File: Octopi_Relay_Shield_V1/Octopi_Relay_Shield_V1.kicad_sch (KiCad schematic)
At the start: 12 parts, among them J1 Raspberry_Pi_2_3, J2 Screw_Terminal_01x03, K1 JQC-3FF-005-1Z, Q1 PNP, U1 LTV-817S

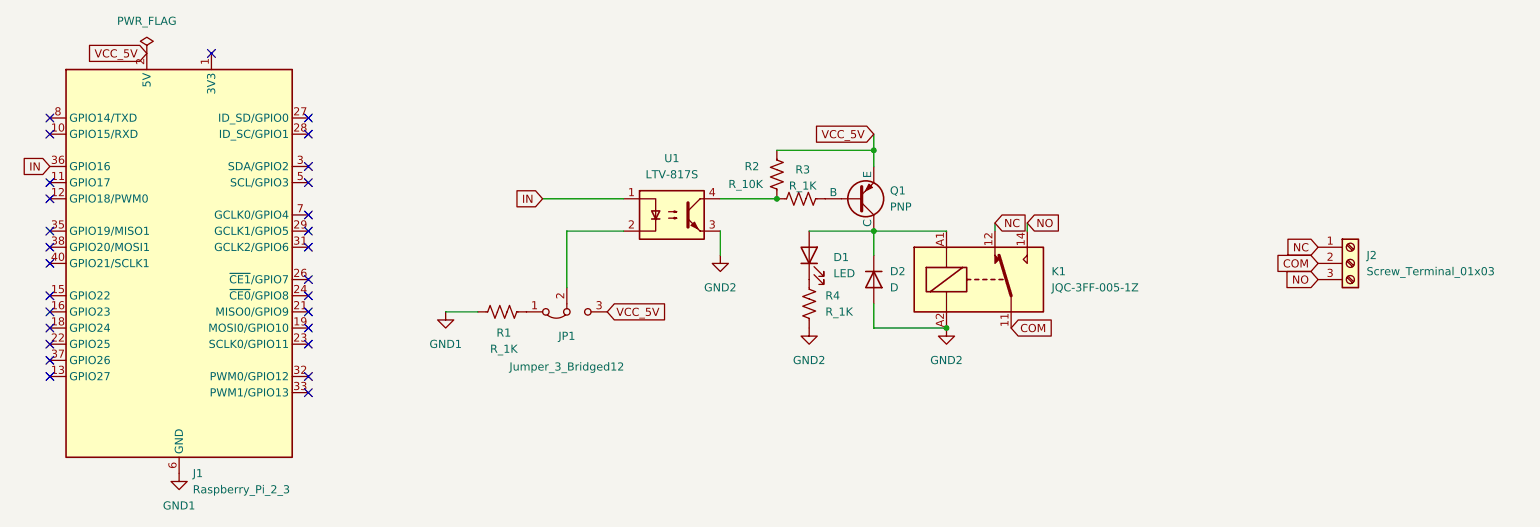
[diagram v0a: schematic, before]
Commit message: Completed Layout for first two designs, generated the fab files
updated the nets, GND1 and GND2 have been joined into just GND1. separated GNDs would only be possible if there was a separate non-pi voltage source for the 5V on the other side of the octocoupler
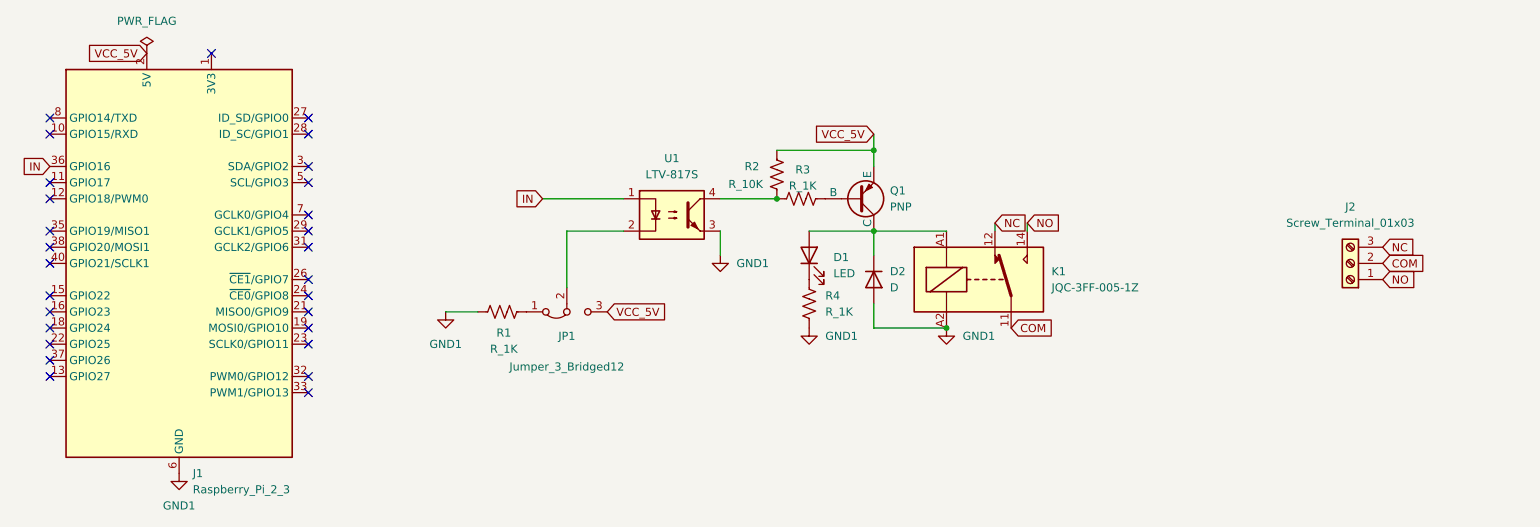
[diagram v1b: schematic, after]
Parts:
- D1: footprint (none) -> LED_SMD:LED_0603_1608Metric_Pad1.05x0.95mm_HandSolder
- D2: footprint (none) -> Diode_THT:D_5W_P12.70mm_Horizontal
- J1: footprint (none) -> Connector_PinSocket_2.54mm:PinSocket_2x20_P2.54mm_Vertical
- J2: footprint (none) -> TerminalBlock_Phoenix:TerminalBlock_Phoenix_PT-1,5-3-5.0-H_1x03_P5.00mm_Horizontal
- JP1: footprint (none) -> Connector_PinHeader_2.54mm:PinHeader_1x03_P2.54mm_Vertical
- Q1: footprint (none) -> Package_TO_SOT_SMD:SOT-23_Handsoldering
- R1, R2, R3, R4: footprint (none) -> Resistor_SMD:R_0805_2012Metric_Pad1.20x1.40mm_HandSolder
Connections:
- net GND2 is gone; now on net GND1: D2.2 (A), K1.A2, R4.2, U1.3
- net NC: now also J2.3 (Pin_3); no longer J2.1 (Pin_1)
- net NO: now also J2.1 (Pin_1); no longer J2.3 (Pin_3)
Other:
- moved on the sheet: J2
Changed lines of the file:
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@@
 	(global_label "COM"
 		(shape input)
-		(at 229.87 74.93 180)
+		(at 240.03 74.93 0)
 		(fields_autoplaced yes)
 		(effects
@@
 				(size 1.27 1.27)
 			)
-			(justify right)
+			(justify left)
 		)
 		(property "Intersheetrefs" "${INTERSHEET_REFS}"
-			(at 222.8329 74.93 0)
-			(effects
-				(font
-					(size 1.27 1.27)
-				)
-				(justify right)
+			(at 247.0671 74.93 0)
+			(effects
+				(font
+					(size 1.27 1.27)
+				)
+				(justify left)
 				(hide yes)
 			)
@@
 	(global_label "NC"
 		(shape input)
-		(at 229.87 72.39 180)
+		(at 240.03 72.39 0)
 		(fields_autoplaced yes)
 		(effects
@@
 				(size 1.27 1.27)
 			)
-			(justify right)
+			(justify left)
 		)
 		(property "Intersheetrefs" "${INTERSHEET_REFS}"
-			(at 224.2843 72.39 0)
-			(effects
-				(font
-					(size 1.27 1.27)
-				)
-				(justify right)
+			(at 245.6157 72.39 0)
+			(effects
+				(font
+					(size 1.27 1.27)
+				)
+				(justify left)
 				(hide yes)
 			)
@@
 	(global_label "NO"
 		(shape input)
-		(at 229.87 77.47 180)
+		(at 240.03 77.47 0)
 		(fields_autoplaced yes)
 		(effects
@@
 				(size 1.27 1.27)
 			)
-			(justify right)
+			(justify left)
 		)
 		(property "Intersheetrefs" "${INTERSHEET_REFS}"
-			(at 224.2238 77.47 0)
-			(effects
-				(font
-					(size 1.27 1.27)
-				)
-				(justify right)
+			(at 245.6762 77.47 0)
+			(effects
+				(font
+					(size 1.27 1.27)
+				)
+				(justify left)
 				(hide yes)
 			)
@@
 			)
 		)
-		(property "Value" "GND2"
-			(at 135.89 78.74 0)
-			(effects
-				(font
-					(size 1.27 1.27)
-				)
+		(property "Value" "GND1"
+			(at 138.43 74.9299 0)
+			(effects
+				(font
+					(size 1.27 1.27)
+				)
+				(justify left)
 			)
 		)
@@
 			)
 		)
-		(property "Footprint" ""
+		(property "Footprint" "Connector_PinHeader_2.54mm:PinHeader_1x03_P2.54mm_Vertical"
 			(at 111.76 82.55 0)
 			(effects
@@
 			)
 		)
-		(property "Footprint" ""
+		(property "Footprint" "Resistor_SMD:R_0805_2012Metric_Pad1.20x1.40mm_HandSolder"
 			(at 150.876 81.534 90)
 			(effects
@@
 			)
 		)
-		(property "Footprint" ""
+		(property "Footprint" "Resistor_SMD:R_0805_2012Metric_Pad1.20x1.40mm_HandSolder"
 			(at 145.796 61.214 90)
 			(effects
@@
 			)
 		)
-		(property "Footprint" ""
+		(property "Footprint" "Resistor_SMD:R_0805_2012Metric_Pad1.20x1.40mm_HandSolder"
 			(at 148.844 63.754 90)
 			(effects
@@
 			)
 		)
-		(property "Value" "GND2"
-			(at 149.86 90.17 0)
-			(effects
-				(font
-					(size 1.27 1.27)
-				)
+		(property "Value" "GND1"
+			(at 152.4 86.3599 0)
+			(effects
+				(font
+					(size 1.27 1.27)
+				)
+				(justify left)
 			)
 		)
@@
 			)
 		)
-		(property "Value" "GND2"
-			(at 171.45 90.17 0)
-			(effects
-				(font
-					(size 1.27 1.27)
-				)
+		(property "Value" "GND1"
+			(at 173.99 86.3599 0)
+			(effects
+				(font
+					(size 1.27 1.27)
+				)
+				(justify left)
 			)
 		)
@@
 	(symbol
 		(lib_id "Connector:Screw_Terminal_01x03")
-		(at 234.95 74.93 0)
+		(at 234.95 74.93 180)
 		(unit 1)
 		(exclude_from_sim no)
@@
 		(fields_autoplaced yes)
 		(property "Reference" "J2"
-			(at 237.49 73.6599 0)
-			(effects
-				(font
-					(size 1.27 1.27)
-				)
-				(justify left)
+			(at 234.95 66.04 0)
+			(effects
+				(font
+					(size 1.27 1.27)
+				)
 			)
 		)
 		(property "Value" "Screw_Terminal_01x03"
-			(at 237.49 76.1999 0)
-			(effects
-				(font
-					(size 1.27 1.27)
-				)
-				(justify left)
-			)
-		)
-		(property "Footprint" ""
+			(at 234.95 68.58 0)
+			(effects
+				(font
+					(size 1.27 1.27)
+				)
+			)
+		)
+		(property "Footprint" "TerminalBlock_Phoenix:TerminalBlock_Phoenix_PT-1,5-3-5.0-H_1x03_P5.00mm_Horizontal"
 			(at 234.95 74.93 0)
 			(effects
@@
 			)
 		)
-		(property "Footprint" ""
+		(property "Footprint" "Resistor_SMD:R_0805_2012Metric_Pad1.20x1.40mm_HandSolder"
 			(at 101.854 81.534 90)
 			(effects
@@
 			)
 		)
-		(property "Footprint" ""
+		(property "Footprint" "Package_TO_SOT_SMD:SOT-23_Handsoldering"
 			(at 193.04 64.77 0)
 			(effects
@@
 			)
 		)
-		(property "Footprint" ""
+		(property "Footprint" "LED_SMD:LED_0603_1608Metric_Pad1.05x0.95mm_HandSolder"
 			(at 149.86 73.66 0)
 			(effects
@@
 			)
 		)
-		(property "Footprint" ""
+		(property "Footprint" "Diode_THT:D_5W_P12.70mm_Horizontal"
 			(at 160.02 77.47 0)
 			(effects
@@
 			)
 		)
-		(property "Footprint" ""
+		(property "Footprint" "Connector_PinSocket_2.54mm:PinSocket_2x20_P2.54mm_Vertical"
 			(at 50.8 74.93 0)
 			(effects
